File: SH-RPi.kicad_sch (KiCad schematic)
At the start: 1 part, among them J101 Conn_01x02

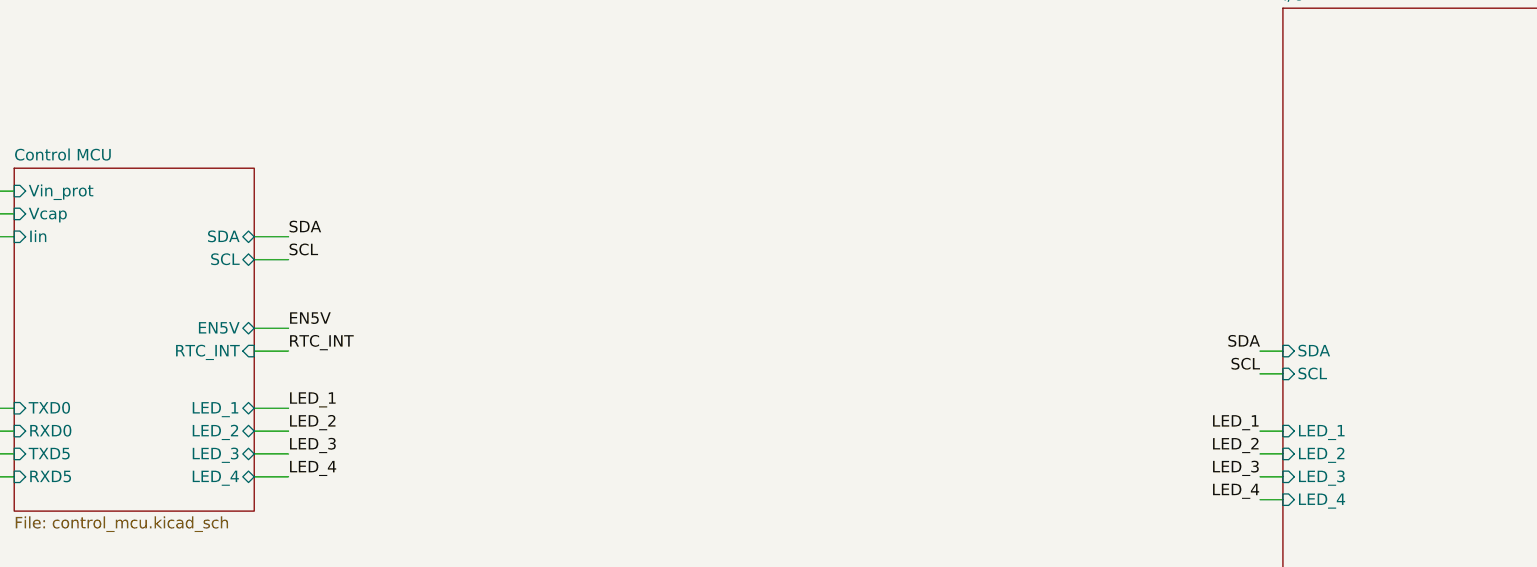
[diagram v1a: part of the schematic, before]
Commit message: Flip the pass through connector to bottom side
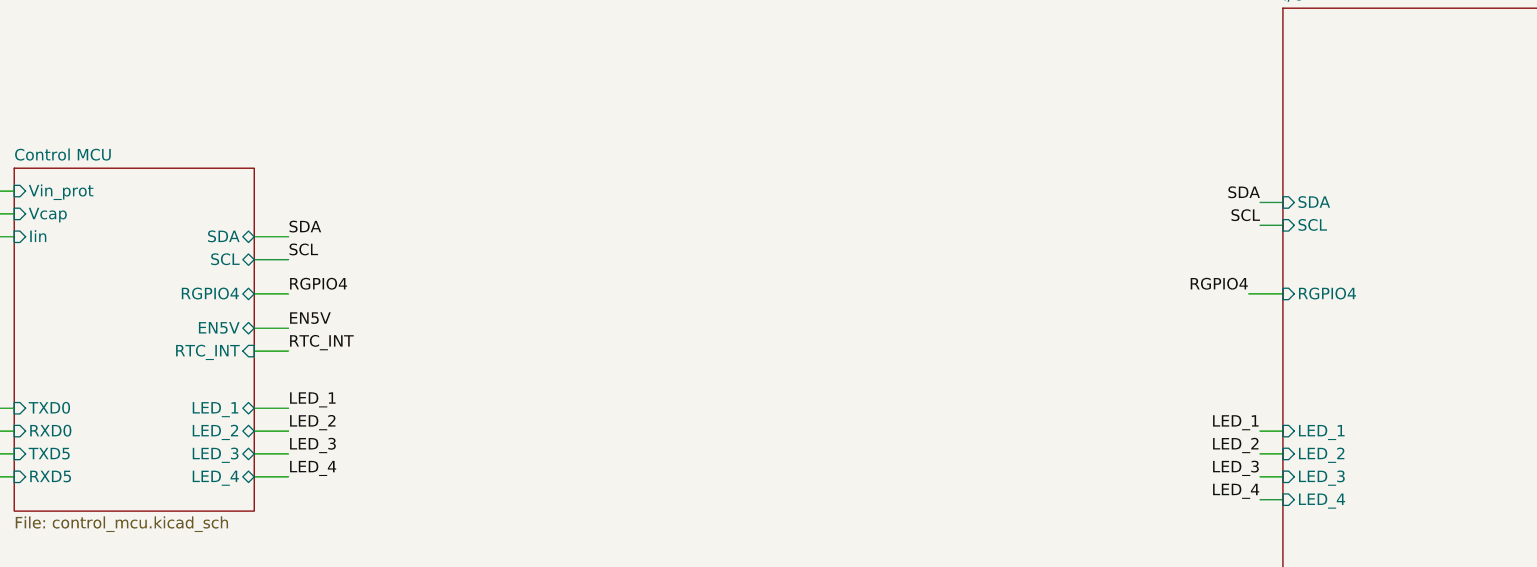
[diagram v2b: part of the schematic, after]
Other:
- sheet Control MCU ports: added RGPIO4; removed none
- sheet I/O ports: added RGPIO4; removed none
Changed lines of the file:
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@@
+    (stroke (width 0) (type default) (color 0 0 0 0))
+  )
+  (wire (pts (xy 232.41 102.87) (xy 228.6 102.87))
     (stroke (width 0) (type default) (color 0 0 0 0))
   )
@@
     (stroke (width 0) (type default) (color 0 0 0 0))
   )
-  (wire (pts (xy 232.41 111.76) (xy 229.87 111.76))
+  (wire (pts (xy 232.41 95.25) (xy 229.87 95.25))
     (stroke (width 0) (type default) (color 0 0 0 0))
   )
@@
     (stroke (width 0) (type default) (color 0 0 0 0))
   )
+  (wire (pts (xy 118.11 102.87) (xy 121.92 102.87))
+    (stroke (width 0) (type default) (color 0 0 0 0))
+  )
   (wire (pts (xy 135.89 33.02) (xy 154.94 33.02))
     (stroke (width 0) (type default) (color 0 0 0 0))
   )
-  (wire (pts (xy 229.87 109.22) (xy 232.41 109.22))
+  (wire (pts (xy 229.87 92.71) (xy 232.41 92.71))
     (stroke (width 0) (type default) (color 0 0 0 0))
   )
@@
     (effects (font (size 1.27 1.27)) (justify left bottom))
   )
-  (label "SCL" (at 229.87 111.76 180)
+  (label "SCL" (at 229.87 95.25 180)
     (effects (font (size 1.27 1.27)) (justify right bottom))
   )
@@
     (effects (font (size 1.27 1.27)) (justify right bottom))
   )
+  (label "RGPIO4" (at 121.92 102.87 0)
+    (effects (font (size 1.27 1.27)) (justify left bottom))
+  )
   (label "Vin_prot" (at 63.5 27.94 0)
     (effects (font (size 1.27 1.27)) (justify left bottom))
@@
     (effects (font (size 1.27 1.27)) (justify left bottom))
   )
-  (label "SDA" (at 229.87 109.22 180)
+  (label "SDA" (at 229.87 92.71 180)
     (effects (font (size 1.27 1.27)) (justify right bottom))
   )
@@
   )
   (label "LED_1" (at 229.87 118.11 180)
+    (effects (font (size 1.27 1.27)) (justify right bottom))
+  )
+  (label "RGPIO4" (at 228.6 102.87 180)
     (effects (font (size 1.27 1.27)) (justify right bottom))
   )
@@
       (effects (font (size 1.27 1.27)) (justify left))
     )
+    (pin "RGPIO4" bidirectional (at 118.11 102.87 0)
+      (effects (font (size 1.27 1.27)) (justify right))
+    )
   )
   (sheet (at 74.93 29.21) (size 19.05 13.97) (fields_autoplaced)
@@
       (effects (font (size 1.27 1.27)) (justify left top))
     )
-    (pin "SDA" input (at 232.41 109.22 180)
-      (effects (font (size 1.27 1.27)) (justify left))
-    )
-    (pin "SCL" input (at 232.41 111.76 180)
+    (pin "SDA" input (at 232.41 92.71 180)
+      (effects (font (size 1.27 1.27)) (justify left))
+    )
+    (pin "SCL" input (at 232.41 95.25 180)
       (effects (font (size 1.27 1.27)) (justify left))
     )
@@
     )
     (pin "TXD0" input (at 232.41 138.43 180)
+      (effects (font (size 1.27 1.27)) (justify left))
+    )
+    (pin "RGPIO4" input (at 232.41 102.87 180)
       (effects (font (size 1.27 1.27)) (justify left))
     )
@@
     )
     (path "/00000000-0000-0000-0000-00005ca73f16/15c4e24c-1a2a-4ae1-8f7d-806cc305bc8d"
-      (reference "D202") (unit 1) (value "SSL54F") (footprint "Diode_SMD:D_SMA")
+      (reference "D202") (unit 1) (value "MSK340A") (footprint "Diode_SMD:D_SMA")
     )
     (path "/00000000-0000-0000-0000-00005ca65cc5/6fdaf3c3-5d6d-4a1f-b928-b1700ab21cf0"
@@
     )
     (path "/00000000-0000-0000-0000-00005fad80e5/00000000-0000-0000-0000-00005fae04f8"
-      (reference "J501") (unit 1) (value "Raspberry_Pi_2_3") (footprint "SH-RPi:PassthroughPinSocket_2x40_P2.54mm_Vertical")
+      (reference "J501") (unit 1) (value "Raspberry_Pi_2_3") (footprint "SH-RPi:PassthroughPinSocket_2x40_P2.54mm_Vertical_Bottom")
     )
     (path "/00000000-0000-0000-0000-00005fad80e5/384ae2ea-c7fc-499b-bf07-3627f4029b52"
@@
       (reference "J801") (unit 1) (value "Conn_01x03") (footprint "SH-RPi:BatteryHolder_Myoung_MY-1220-03")
     )
+    (path "/00000000-0000-0000-0000-00005fad80e5/043911e3-d8fa-4877-8f7b-a1eb08ae876c"
+      (reference "JP501") (unit 1) (value "Open") (footprint "Jumper:SolderJumper-2_P1.3mm_Open_TrianglePad1.0x1.5mm")
+    )
     (path "/00000000-0000-0000-0000-00005d6f1c7c/41f9fe4b-2a85-4c88-b1a9-6058d8b40c8f"
